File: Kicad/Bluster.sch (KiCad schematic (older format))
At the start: 10 parts, among them J1 Buster, J2 Buster, U1 Buster, U2 TC1262-3.3V

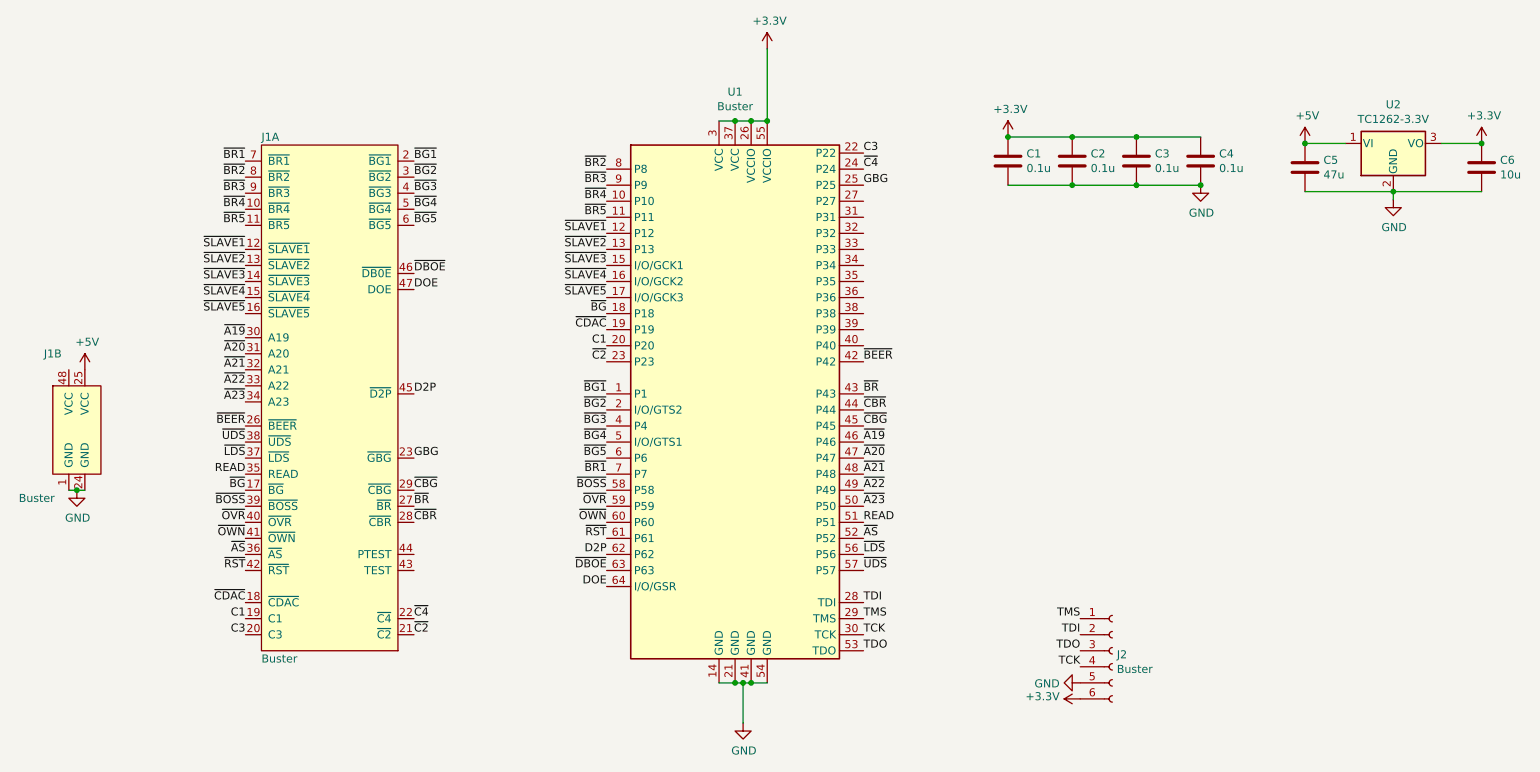
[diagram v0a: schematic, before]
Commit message: Re-do PCB to fit within standard DIP footprint
Fixes #1
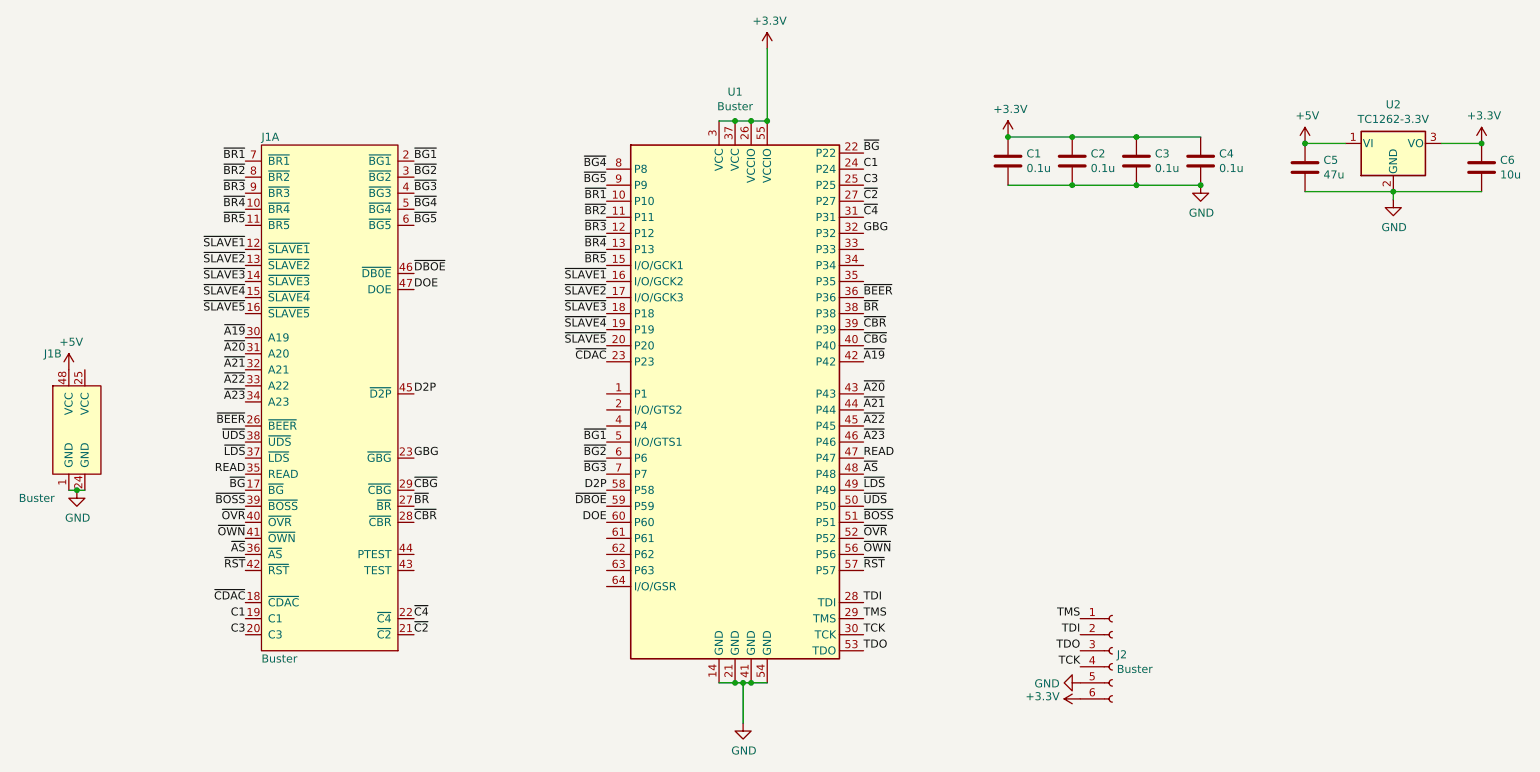
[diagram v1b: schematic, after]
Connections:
- net +5V: now also J1.48 (VCC); no longer J1.25 (VCC)
- net C1: now also U1.24 (P24); no longer U1.20 (P20)
- net C3: now also U1.25 (P25); no longer U1.22 (P22)
- net D2P: now also U1.58 (P58); no longer U1.62 (P62)
- net DOE: now also U1.60 (P60); no longer U1.64 (I/O/GSR)
- net GBG: now also U1.32 (P32); no longer U1.25 (P25)
- net READ: now also U1.47 (P47); no longer U1.51 (P51)
- net ~A19: now also U1.42 (P42); no longer U1.46 (P46)
- net ~A20: now also U1.43 (P43); no longer U1.47 (P47)
- net ~A21: now also U1.44 (P44); no longer U1.48 (P48)
- net ~A22: now also U1.45 (P45); no longer U1.49 (P49)
- net ~A23: now also U1.46 (P46); no longer U1.50 (P50)
- net ~AS: now also U1.48 (P48); no longer U1.52 (P52)
- net ~BEER: now also U1.36 (P36); no longer U1.42 (P42)
- net ~BG: now also U1.22 (P22); no longer U1.18 (P18)
- net ~BG1: now also U1.5 (I/O/GTS1); no longer U1.1 (P1)
- net ~BG2: now also U1.6 (P6); no longer U1.2 (I/O/GTS2)
- net ~BG3: now also U1.7 (P7); no longer U1.4 (P4)
- net ~BG4: now also U1.8 (P8); no longer U1.5 (I/O/GTS1)
- net ~BG5: now also U1.9 (P9); no longer U1.6 (P6)
- net ~BOSS: now also U1.51 (P51); no longer U1.58 (P58)
- net ~BR: now also U1.38 (P38); no longer U1.43 (P43)
- net ~BR1: now also U1.10 (P10); no longer U1.7 (P7)
- net ~BR2: now also U1.11 (P11); no longer U1.8 (P8)
- net ~BR3: now also U1.12 (P12); no longer U1.9 (P9)
- net ~BR4: now also U1.13 (P13); no longer U1.10 (P10)
- net ~BR5: now also U1.15 (I/O/GCK1); no longer U1.11 (P11)
- net ~C2: now also U1.27 (P27); no longer U1.23 (P23)
- net ~C4: now also U1.31 (P31); no longer U1.24 (P24)
- net ~CBG: now also U1.40 (P40); no longer U1.45 (P45)
- net ~CBR: now also U1.39 (P39); no longer U1.44 (P44)
- net ~CDAC: now also U1.23 (P23); no longer U1.19 (P19)
- net ~DBOE: now also U1.59 (P59); no longer U1.63 (P63)
- net ~LDS: now also U1.49 (P49); no longer U1.56 (P56)
- net ~OVR: now also U1.52 (P52); no longer U1.59 (P59)
- net ~OWN: now also U1.56 (P56); no longer U1.60 (P60)
- net ~RST: now also U1.57 (P57); no longer U1.61 (P61)
- net ~SLAVE1: now also U1.16 (I/O/GCK2); no longer U1.12 (P12)
- net ~SLAVE2: now also U1.17 (I/O/GCK3); no longer U1.13 (P13)
- net ~SLAVE3: now also U1.18 (P18); no longer U1.15 (I/O/GCK1)
- net ~SLAVE4: now also U1.19 (P19); no longer U1.16 (I/O/GCK2)
- net ~SLAVE5: now also U1.20 (P20); no longer U1.17 (I/O/GCK3)
- net ~UDS: now also U1.50 (P50); no longer U1.57 (P57)
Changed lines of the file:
@@
 L power:+5V #PWR02
 U 1 1 601644A8
-P 1550 2800
-F 0 "#PWR02" H 1550 2650 50  0001 C CNN
-F 1 "+5V" H 1565 2973 50  0000 C CNN
-F 2 "" H 1550 2800 50  0001 C CNN
-F 3 "" H 1550 2800 50  0001 C CNN
-	1    1550 2800
+P 1450 2800
+F 0 "#PWR02" H 1450 2650 50  0001 C CNN
+F 1 "+5V" H 1465 2973 50  0000 C CNN
+F 2 "" H 1450 2800 50  0001 C CNN
+F 3 "" H 1450 2800 50  0001 C CNN
+	1    1450 2800
 	1    0    0    -1
 $EndComp
-Text Label 4800 2950 2    50   ~ 0
+Text Label 4800 3250 2    50   ~ 0
 ~BG1
-Text Label 4800 3050 2    50   ~ 0
+Text Label 4800 3350 2    50   ~ 0
 ~BG2
-Text Label 4800 3150 2    50   ~ 0
+Text Label 4800 3450 2    50   ~ 0
 ~BG3
-Text Label 4800 3250 2    50   ~ 0
+Text Label 4800 1550 2    50   ~ 0
 ~BG4
-Text Label 4800 3350 2    50   ~ 0
+Text Label 4800 1650 2    50   ~ 0
 ~BG5
-Text Label 4800 3450 2    50   ~ 0
+Text Label 4800 1750 2    50   ~ 0
 ~BR1
-Text Label 4800 1550 2    50   ~ 0
+Text Label 4800 1850 2    50   ~ 0
 ~BR2
-Text Label 4800 1650 2    50   ~ 0
+Text Label 4800 1950 2    50   ~ 0
 ~BR3
-Text Label 4800 1750 2    50   ~ 0
+Text Label 4800 2050 2    50   ~ 0
 ~BR4
-Text Label 4800 1850 2    50   ~ 0
+Text Label 4800 2150 2    50   ~ 0
 ~BR5
-Text Label 4800 1950 2    50   ~ 0
+Text Label 4800 2250 2    50   ~ 0
 ~SLAVE1
-Text Label 4800 2050 2    50   ~ 0
+Text Label 4800 2350 2    50   ~ 0
 ~SLAVE2
-Text Label 4800 2150 2    50   ~ 0
+Text Label 4800 2450 2    50   ~ 0
 ~SLAVE3
-Text Label 4800 2250 2    50   ~ 0
+Text Label 4800 2550 2    50   ~ 0
 ~SLAVE4
-Text Label 4800 2350 2    50   ~ 0
+Text Label 4800 2650 2    50   ~ 0
 ~SLAVE5
-Text Label 4800 2450 2    50   ~ 0
+Text Label 6400 1450 0    50   ~ 0
 ~BG
-Text Label 4800 2550 2    50   ~ 0
+Text Label 4800 2750 2    50   ~ 0
 ~CDAC
-Text Label 4800 2650 2    50   ~ 0
+Text Label 6400 1550 0    50   ~ 0
 C1
-Text Label 6400 1450 0    50   ~ 0
+Text Label 6400 1650 0    50   ~ 0
 C3
-Text Label 4800 2750 2    50   ~ 0
+Text Label 6400 1750 0    50   ~ 0
 ~C2
-Text Label 6400 1550 0    50   ~ 0
+Text Label 6400 1850 0    50   ~ 0
 ~C4
-Text Label 6400 1650 0    50   ~ 0
+Text Label 6400 1950 0    50   ~ 0
 GBG
-Text Label 4800 4150 2    50   ~ 0
+Text Label 4800 3750 2    50   ~ 0
 DOE
-Text Label 4800 4050 2    50   ~ 0
+Text Label 4800 3650 2    50   ~ 0
 ~DBOE
-Text Label 4800 3950 2    50   ~ 0
+Text Label 4800 3550 2    50   ~ 0
 D2P
-Text Label 4800 3850 2    50   ~ 0
+Text Label 6400 4050 0    50   ~ 0
 ~RST
-Text Label 4800 3750 2    50   ~ 0
+Text Label 6400 3950 0    50   ~ 0
 ~OWN
-Text Label 4800 3650 2    50   ~ 0
+Text Label 6400 3850 0    50   ~ 0
 ~OVR
-Text Label 4800 3550 2    50   ~ 0
+Text Label 6400 3750 0    50   ~ 0
 ~BOSS
-Text Label 6400 4050 0    50   ~ 0
+Text Label 6400 3650 0    50   ~ 0
 ~UDS
-Text Label 6400 3950 0    50   ~ 0
+Text Label 6400 3550 0    50   ~ 0
 ~LDS
-Text Label 6400 3850 0    50   ~ 0
+Text Label 6400 3450 0    50   ~ 0
 ~AS
-Text Label 6400 3750 0    50   ~ 0
+Text Label 6400 3350 0    50   ~ 0
 READ
-Text Label 6400 3650 0    50   ~ 0
+Text Label 6400 3250 0    50   ~ 0
 ~A23
-Text Label 6400 3550 0    50   ~ 0
+Text Label 6400 3150 0    50   ~ 0
 ~A22
-Text Label 6400 3450 0    50   ~ 0
+Text Label 6400 3050 0    50   ~ 0
 ~A21
-Text Label 6400 3350 0    50   ~ 0
+Text Label 6400 2950 0    50   ~ 0
 ~A20
-Text Label 6400 3250 0    50   ~ 0
+Text Label 6400 2750 0    50   ~ 0
 ~A19
-Text Label 6400 3150 0    50   ~ 0
+Text Label 6400 2650 0    50   ~ 0
 ~CBG
-Text Label 6400 3050 0    50   ~ 0
+Text Label 6400 2550 0    50   ~ 0
 ~CBR
-Text Label 6400 2950 0    50   ~ 0
+Text Label 6400 2450 0    50   ~ 0
 ~BR
-Text Label 6400 2750 0    50   ~ 0
+Text Label 6400 2350 0    50   ~ 0
 ~BEER
 $EndSCHEMATC
